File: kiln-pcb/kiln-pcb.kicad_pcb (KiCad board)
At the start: 2 copper layers, 91.4 x 55.9 mm, 12 parts, among them J1 TFT, J2 Temp, J3 Rotary, J4 Relay, U1 WeMos_D1_mini

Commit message: Added simple PID for relay
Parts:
- H1, H2, H3, H4: footprint MountingHole:MountingHole_3.2mm_M3 -> MountingHole:MountingHole_3.2mm_M3_Pad_Via
- J2: value Temp -> TEMP
- J3: value Rotary -> ROTARY
- TP1: value 5V -> 5V test
- TP2: value GND -> GND test

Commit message: PCB v1.1
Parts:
- added J5: Relay, Connector_PinHeader_2.54mm:PinHeader_1x03_P2.54mm_Vertical, F.Cu at (137.2, 83.8)
- added J6: Relay, Connector_PinHeader_2.54mm:PinHeader_1x03_P2.54mm_Vertical, F.Cu at (137.2, 104.1)
- added REF**: OSHW-Logo2_9.8x8mm_Copper, Symbol:OSHW-Logo2_9.8x8mm_Copper, F.Cu at (156.2, 45.7)
- added Ref**: Val**, wemos_d1_mini:hackspace_small, F.Cu at (141.0, 44.5)
- TP1: value 5V test -> 5V
- TP2: value GND test -> GND
- TP3: value Relay signal -> SIG
- moved TP1 73.3 mm to (92.7, 57.1)
- moved TP2 64.2 mm to (99.1, 57.1)
- moved TP3 57.5 mm to (104.1, 57.1)
- moved U1 37.6 mm to (109.2, 91.4), turned to 180 degrees
- moved J4 28.9 mm to (137.2, 63.5), turned to 180 degrees
- moved J1 24.4 mm to (87.6, 119.4)
- moved J3 24.4 mm to (128.3, 119.4)
- moved H1 20.7 mm to (171.4, 116.8)
- moved H2 18.1 mm to (171.4, 44.5)
- moved H3 15.7 mm to (80.0, 116.8)
- moved H4 12.0 mm to (80.0, 44.5)
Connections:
- J1 pad 2: CS_T -> CS_TFT
- U1 pad 16: unconnected-(U1-Pad16) -> CS_T
- U1 pad 7: CS_T -> CS_TFT
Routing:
- net GND_ROTARY: track 81.7 -> 190.6 mm, vias 1 -> 0
- net CS_TFT: track 0.00 -> 77.3 mm
- net CS_T: track 105.0 -> 40.1 mm
- net VCC_ROTARY: track 67.1 -> 108.0 mm, vias 1 -> 0
- net SDA_TFT: track 52.0 -> 85.0 mm
- net SO_T: track 53.2 -> 22.2 mm, vias 1 -> 0
- net Sig_relay: track 89.6 -> 108.5 mm, vias 1 -> 0
- net DT_ROTARY: track 75.3 -> 60.0 mm
- net SCK_T: track 76.4 -> 62.6 mm, vias 0 -> 1
- net Vcc_relay: track 64.1 -> 74.2 mm, vias 1 -> 0
- net DC_TFT: track 34.2 -> 42.9 mm
- net RES_TFT: track 53.8 -> 48.8 mm, vias 0 -> 1
- net CLK_ROTARY: track 62.0 -> 66.3 mm
- net SW_ROTARY: track 59.4 -> 61.3 mm
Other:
- board size 91.4 x 55.9 mm -> 101.6 x 82.6 mm
- board text added: "Kiln PCB v1.1 D Goldwater & T Veness https://github.com/tveness/open-kiln"
- board text removed: "Kiln PCB v1 D Goldwater & T Veness https://github.com/tveness/open-kiln"

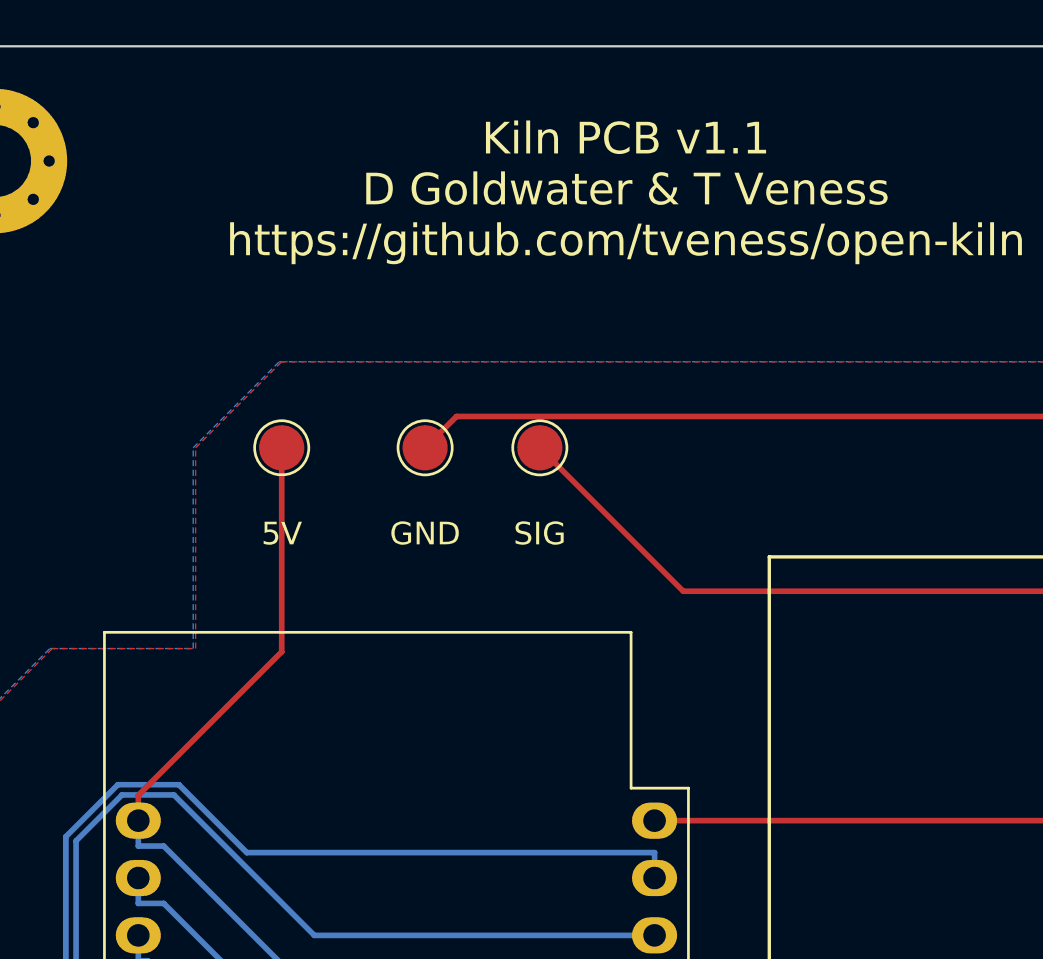
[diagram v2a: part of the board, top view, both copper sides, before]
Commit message: Fixed "kerning"
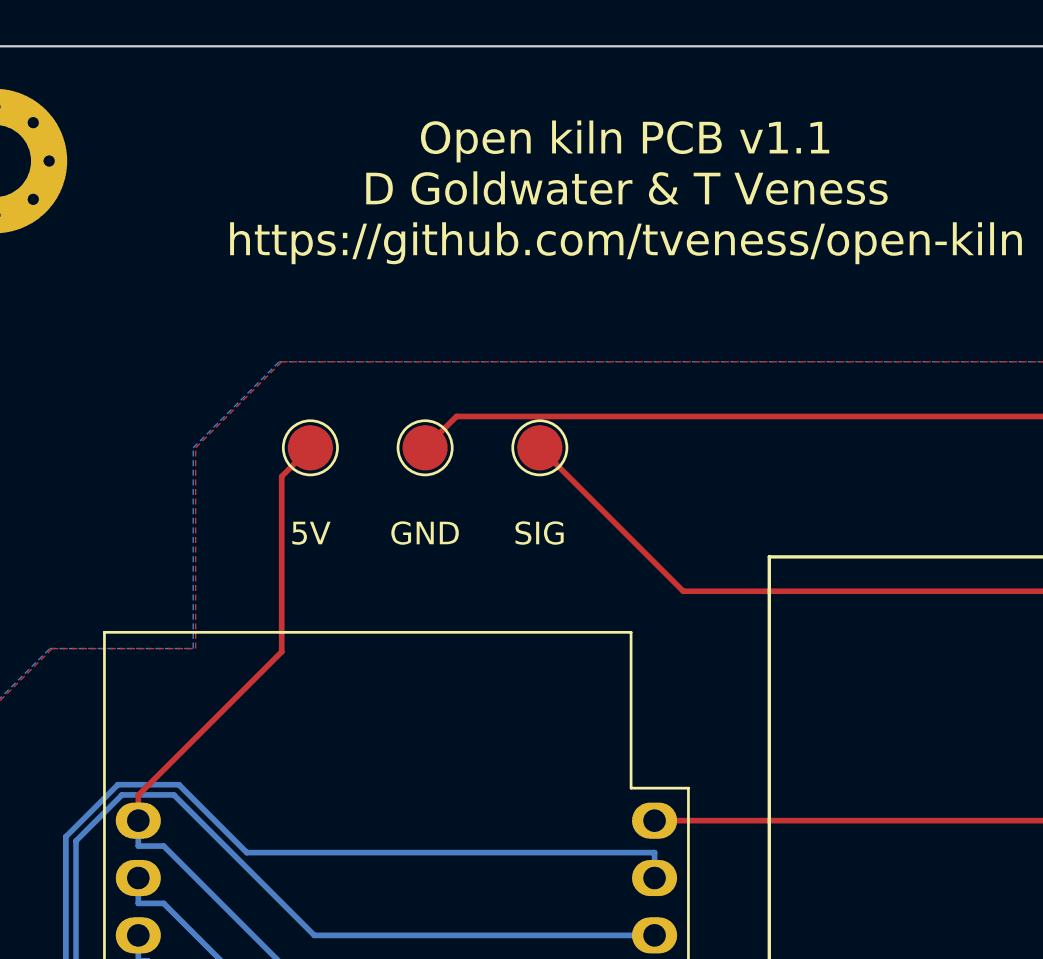
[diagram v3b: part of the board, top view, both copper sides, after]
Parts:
- moved TP1 1.27 mm to (94.0, 57.1)
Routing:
- net VCC_ROTARY: track 108.0 -> 108.6 mm
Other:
- board text added: "Open kiln PCB v1.1 D Goldwater & T Veness https://github.com/tveness/open-kiln"
- board text removed: "Kiln PCB v1.1 D Goldwater & T Veness https://github.com/tveness/open-kiln"
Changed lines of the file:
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@@
   )
   (footprint "TestPoint:TestPoint_Pad_D2.0mm" (layer "F.Cu")
-    (at 92.71 57.15)
+    (at 93.98 57.15)
     (descr "SMD pad as test Point, diameter 2.0mm")
     (tags "test point SMD pad")
@@
     (effects (font (size 0.5 0.5) (thickness 0.125)))
   )
-  (gr_text "Kiln PCB v1.1\nD Goldwater & T Veness\nhttps://github.com/tveness/open-kiln" (at 107.95 45.72) (layer "F.SilkS")
+  (gr_text "Open kiln PCB v1.1\nD Goldwater & T Veness\nhttps://github.com/tveness/open-kiln" (at 107.95 45.72) (layer "F.SilkS")
     (effects (font (size 1.4 1.4) (thickness 0.15)))
   )
@@
   (segment (start 85.6386 72.5207) (end 83.6011 74.5582) (width 0.25) (layer "B.Cu") (net 8))
   (segment (start 109.22 78.74) (end 94.1537 78.74) (width 0.25) (layer "B.Cu") (net 8))
+  (segment (start 92.71 66.1847) (end 86.36 72.5347) (width 0.25) (layer "F.Cu") (net 9))
   (segment (start 120.645 119.38) (end 119.4697 119.38) (width 0.25) (layer "F.Cu") (net 9))
   (segment (start 119.4697 119.7473) (end 118.6617 120.5553) (width 0.25) (layer "F.Cu") (net 9))
   (segment (start 119.4697 119.38) (end 119.4697 119.7473) (width 0.25) (layer "F.Cu") (net 9))
   (segment (start 104.0453 119.7474) (end 104.0453 119.38) (width 0.25) (layer "F.Cu") (net 9))
-  (segment (start 86.36 73.66) (end 86.36 72.5347) (width 0.25) (layer "F.Cu") (net 9))
-  (segment (start 92.71 66.1847) (end 86.36 72.5347) (width 0.25) (layer "F.Cu") (net 9))
   (segment (start 102.87 119.38) (end 104.0453 119.38) (width 0.25) (layer "F.Cu") (net 9))
+  (segment (start 93.98 57.15) (end 92.71 58.42) (width 0.25) (layer "F.Cu") (net 9))
+  (segment (start 86.36 72.5347) (end 86.36 73.66) (width 0.25) (layer "F.Cu") (net 9))
   (segment (start 104.8532 120.5553) (end 104.0453 119.7474) (width 0.25) (layer "F.Cu") (net 9))
+  (segment (start 92.71 58.42) (end 92.71 66.1847) (width 0.25) (layer "F.Cu") (net 9))
   (segment (start 118.6617 120.5553) (end 104.8532 120.5553) (width 0.25) (layer "F.Cu") (net 9))
-  (segment (start 92.71 57.15) (end 92.71 66.1847) (width 0.25) (layer "F.Cu") (net 9))
   (segment (start 86.36 74.7853) (end 87.4853 74.7853) (width 0.25) (layer "B.Cu") (net 9))
   (segment (start 119.38 116.9397) (end 120.645 118.2047) (width 0.25) (layer "B.Cu") (net 9))
@@
   (segment (start 118.105 119.38) (end 105.41 119.38) (width 0.25) (layer "F.Cu") (net 14))
   (segment (start 118.0153 91.8073) (end 118.0153 91.44) (width 0.25) (layer "F.Cu") (net 14))
+  (segment (start 100.4483 55.7617) (end 99.06 57.15) (width 0.25) (layer "F.Cu") (net 14))
+  (segment (start 136.0447 60.96) (end 130.8464 55.7617) (width 0.25) (layer "F.Cu") (net 14))
+  (segment (start 137.22 101.585) (end 127.793 101.585) (width 0.25) (layer "F.Cu") (net 14))
+  (segment (start 116.84 91.44) (end 118.0153 91.44) (width 0.25) (layer "F.Cu") (net 14))
   (segment (start 137.22 60.96) (end 136.0447 60.96) (width 0.25) (layer "F.Cu") (net 14))
   (segment (start 130.8464 55.7617) (end 100.4483 55.7617) (width 0.25) (layer "F.Cu") (net 14))
-  (segment (start 100.4483 55.7617) (end 99.06 57.15) (width 0.25) (layer "F.Cu") (net 14))
-  (segment (start 137.22 101.585) (end 127.793 101.585) (width 0.25) (layer "F.Cu") (net 14))
-  (segment (start 116.84 91.44) (end 118.0153 91.44) (width 0.25) (layer "F.Cu") (net 14))
-  (segment (start 136.0447 60.96) (end 130.8464 55.7617) (width 0.25) (layer "F.Cu") (net 14))
   (segment (start 116.2524 91.44) (end 115.6647 91.44) (width 0.25) (layer "B.Cu") (net 14))
   (segment (start 137.5874 80.1047) (end 138.3953 79.2968) (width 0.25) (layer "B.Cu") (net 14))

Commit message: Basic README update
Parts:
- removed H1, H2, H3, H4: MountingHole, MountingHole:MountingHole_3.2mm_M3_Pad_Via
- added REF**: MountingHole_3.2mm_M3_Pad_Via, MountingHole:MountingHole_3.2mm_M3_Pad_Via, F.Cu at (171.4, 44.5)
- added REF**: MountingHole_3.2mm_M3_Pad_Via, MountingHole:MountingHole_3.2mm_M3_Pad_Via, F.Cu at (80.0, 116.8)
- added REF**: MountingHole_3.2mm_M3_Pad_Via, MountingHole:MountingHole_3.2mm_M3_Pad_Via, F.Cu at (171.4, 116.8)
- added REF**: MountingHole_3.2mm_M3_Pad_Via, MountingHole:MountingHole_3.2mm_M3_Pad_Via, F.Cu at (80.0, 44.5)
- TP3: value SIG -> Relay
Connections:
- net GND_ROTARY renamed GND_relay
- net VCC_ROTARY renamed 5V
- net Vcc_relay renamed 3V3
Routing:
- net RES_TFT: track 48.8 -> 69.4 mm, vias 1 -> 0
- net 5V: track 108.6 -> 126.1 mm
- net SCK_T: track 62.6 -> 53.0 mm, vias 1 -> 0
- net SW_ROTARY: track 61.3 -> 69.2 mm
- net SDA_TFT: track 85.0 -> 79.0 mm
- net CLK_ROTARY: track 66.3 -> 71.7 mm
- net DT_ROTARY: track 60.0 -> 65.5 mm
- net GND_relay: track 190.6 -> 186.2 mm
- net CS_TFT: track 77.3 -> 73.5 mm
- net Sig_relay: track 108.5 -> 106.8 mm
- net 3V3: track 74.2 -> 73.5 mm

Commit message: Added magnetic switch interrupt
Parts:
- added M-switch: Magnetic, TerminalBlock:TerminalBlock_bornier-2_P5.08mm, F.Cu at (135.9, 44.5)
- moved HS_LOGO 7.62 mm to (148.6, 44.5)
- moved OSHW_LOGO 3.81 mm to (160.0, 45.7)
- renumbered REF** to H1, REF** to H2, REF** to H3, REF** to H4, Ref** to HS_LOGO, REF** to OSHW_LOGO
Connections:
- net GND_relay renamed GND
- J4 pad 3: 3V3 -> RELAY_VCC
- J5 pad 3: 3V3 -> RELAY_VCC
- J6 pad 3: 3V3 -> RELAY_VCC
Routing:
- net RELAY_VCC: track 0.00 -> 59.1 mm
- net 3V3: track 73.5 -> 40.5 mm
- net RES_TFT: track 69.4 -> 40.7 mm, vias 0 -> 1
- net 5V: track 126.1 -> 108.6 mm
- net GND: track 186.2 -> 173.6 mm, vias 0 -> 1
- net SDA_TFT: track 79.0 -> 68.9 mm
- net CS_TFT: track 73.5 -> 65.1 mm
- net SCK_T: track 53.0 -> 55.4 mm
- net Sig_relay: track 106.8 -> 108.5 mm
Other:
- board text added: "Open kiln PCB v1.2 D Goldwater & T Veness https://github.com/tveness/open-kiln"
- board text added: "ROTARY"
- board text added: "TFT"
- board text removed: "Open kiln PCB v1.1 D Goldwater & T Veness https://github.com/tveness/open-kiln"
